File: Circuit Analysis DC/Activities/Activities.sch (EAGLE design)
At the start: 9 parts, among them U1 SWITCH-SPST-2TV

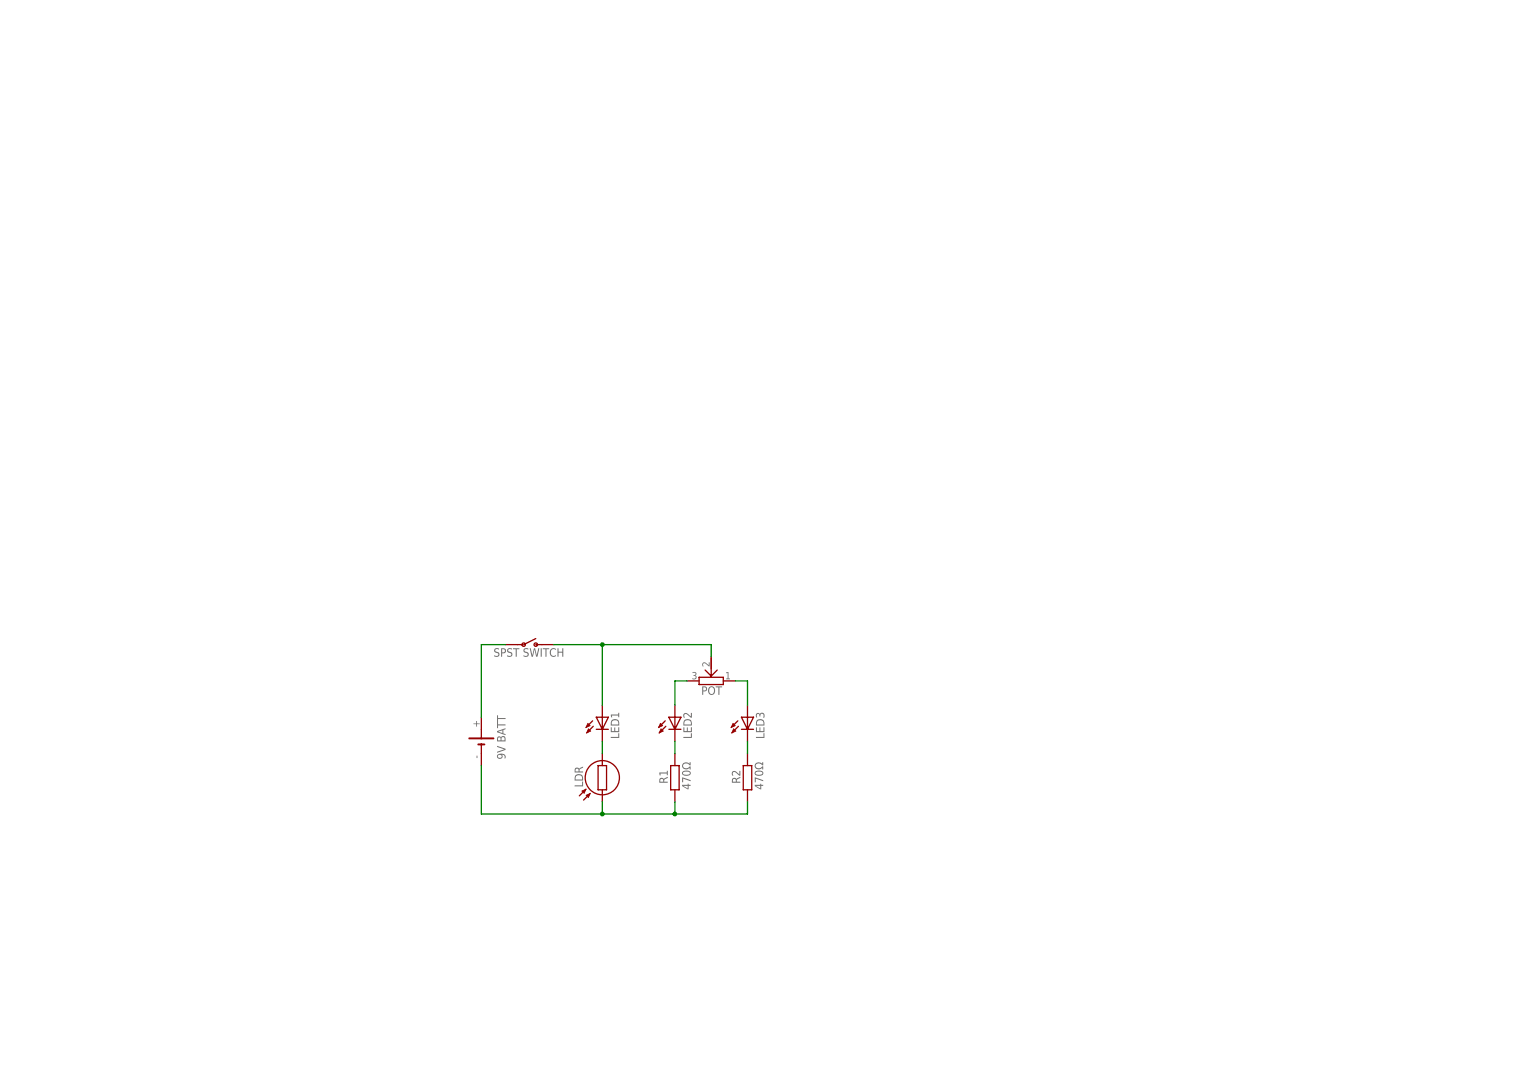
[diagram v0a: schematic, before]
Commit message: added descriptions and thumbnails for website
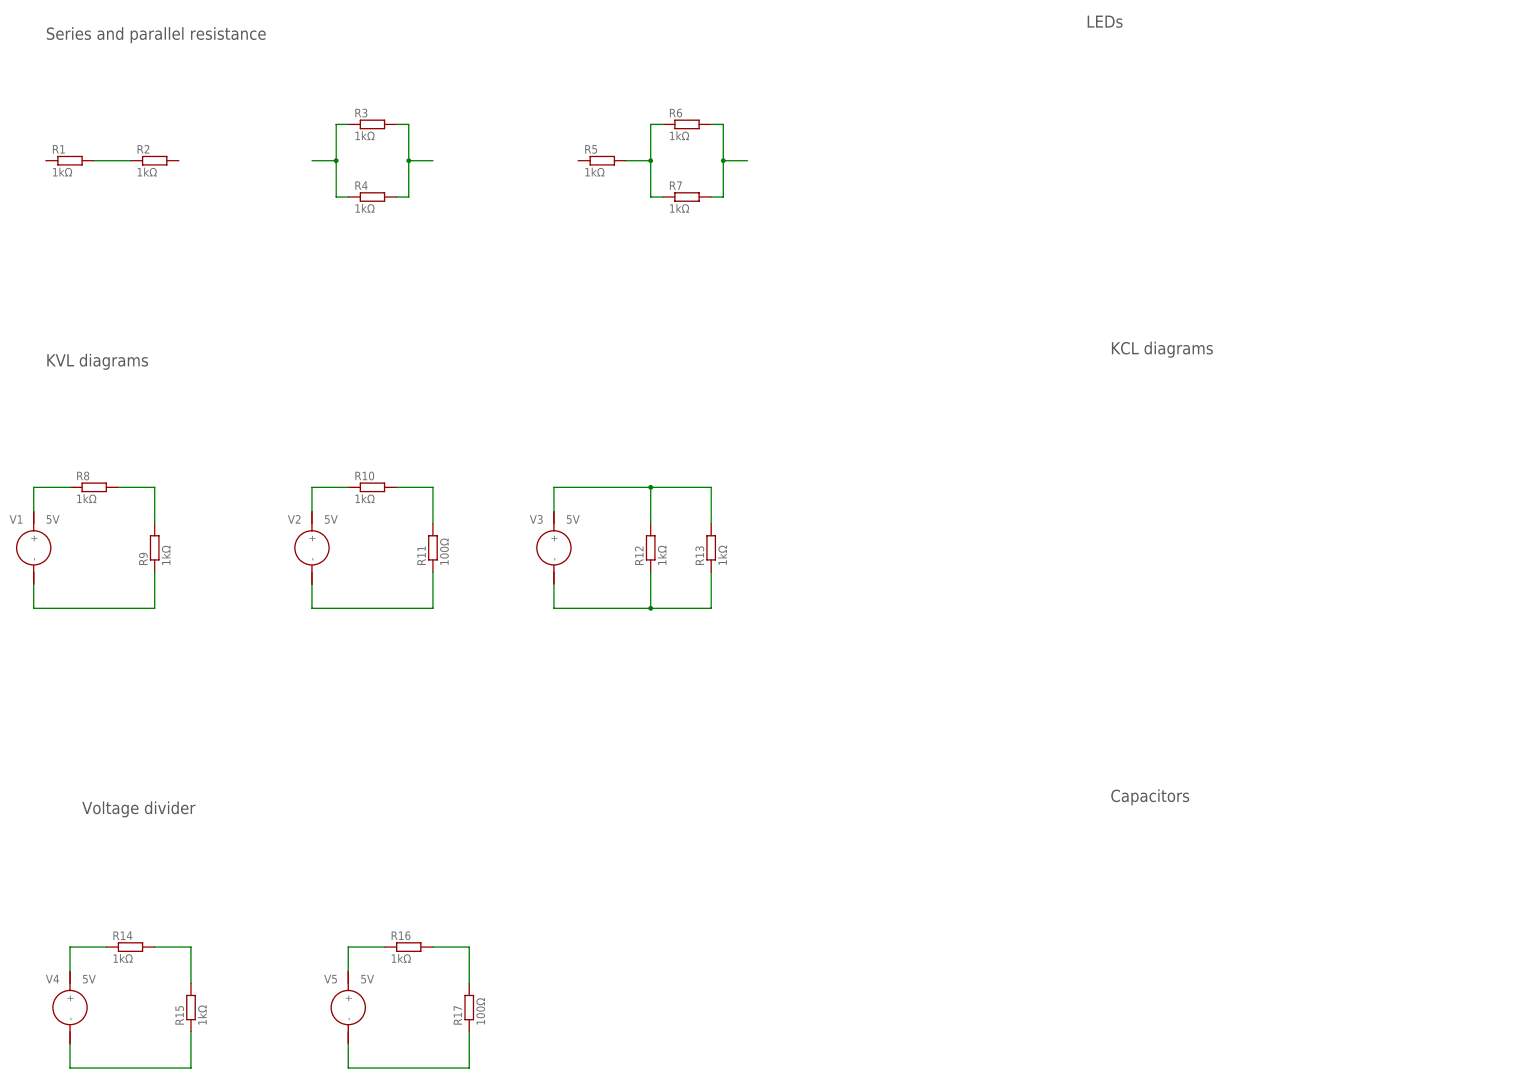
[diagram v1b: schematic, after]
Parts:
- removed G1: BATT_9V, personal:BATT_9V
- removed LDR: LDR_THRU, personal:LDR_THRU
- removed LED1, LED2, LED3: (no value), adafruit:LED5MM
- removed POT: POTENTIOMETER_THRU, personal:POTENTIOMETER_THRU
- removed U1: SWITCH-SPST-2TV, personal:SWITCH-SPST-2TV
- added R10, R12, R13, R14, R15, R16, R3, R4, R5, R6, R7, R8, R9: 1kΩ, rcl:R-EU_0207/10
- added R11, R17: 100Ω, rcl:R-EU_0207/10
- added V1, V2, V3, V4, V5: 5V, personal:VOLTAGE_SOURCE
- R1, R2: value 470Ω -> 1kΩ; device resistor:R-EU_0207/10 -> rcl:R-EU_0207/10
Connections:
- new net N$11: R10.1, V2.+
- new net N$12: R12.2, R13.2, V3.+
- new net N$13: R12.1, R13.1, V3.-
- new net N$14: R14.1, V4.+
- new net N$15: R14.2, R15.2
- new net N$16: R15.1, V4.-
- new net N$17: R17.1, V5.-
- new net N$18: R16.2, R17.2
- new net N$19: R16.1, V5.+
- new net N$4: R5.2, R6.1, R7.1
- new net N$8: R9.1, V1.-
- net N$1: now also R1.2; no longer G1.-, LDR.1, R1.1
- net N$10: now also R10.2, R11.2; no longer LED2.C, R1.2
- net N$2: now also R3.1, R4.1; no longer LED1.A, POT.2, U1.O
- net N$3: now also R3.2, R4.2; no longer LDR.2, LED1.C
- net N$5: now also R6.2, R7.2; no longer LED3.C, R2.2
- net N$6: now also R8.1, V1.+; no longer LED3.A, POT.1
- net N$7: now also R8.2, R9.2; no longer LED2.A, POT.3
- net N$9: now also R11.1, V2.-; no longer G1.+, U1.P
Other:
- note added: "Capacitors"
- note added: "KCL diagrams"
- note added: "KVL diagrams"
- note added: "LEDs"
- note added: "Series and parallel resistance"
- note added: "Voltage divider"
- note removed: "9V BATT"
- note removed: "SPST SWITCH"
- moved on the sheet: R1, R2

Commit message: changed schematic and code
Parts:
- added C1: (no value), rcl:C-EU025-025X050
- added LED1, LED2: (no value), led:LED3MM
- added R18, R19, R20, R22: 1kΩ, rcl:R-EU_0207/10
- added R21: 10kΩ, rcl:R-EU_0207/10
- added U$1: SPDT, another:SPDT
- added V6, V7, V8: 5V, personal:VOLTAGE_SOURCE
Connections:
- new net N$20: R22.2, U$1.B, V8.-
- new net N$21: U$1.IN, V8.+
- new net N$22: C1.1, U$1.A
- new net N$23: C1.2, LED1.A, LED2.C
- new net N$25: LED1.C, LED2.A, R22.1
- new net N$26: R18.2, R19.2, V6.+
- new net N$27: R18.1, R19.1, V6.-
- new net N$28: R20.2, R21.2, V7.+
- new net N$29: R20.1, R21.1, V7.-
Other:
- note added: "SPST SWITCH"
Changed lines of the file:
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@@
 <part name="V4" library="personal" deviceset="VOLTAGE_SOURCE" device="" value="5V"/>
 <part name="V5" library="personal" deviceset="VOLTAGE_SOURCE" device="" value="5V"/>
+<part name="R18" library="rcl" deviceset="R-EU_" device="0207/10" value="1kΩ"/>
+<part name="R19" library="rcl" deviceset="R-EU_" device="0207/10" value="1kΩ"/>
+<part name="R20" library="rcl" deviceset="R-EU_" device="0207/10" value="1kΩ"/>
+<part name="R21" library="rcl" deviceset="R-EU_" device="0207/10" value="10kΩ"/>
+<part name="R22" library="rcl" deviceset="R-EU_" device="0207/10" value="1kΩ"/>
+<part name="V6" library="personal" deviceset="VOLTAGE_SOURCE" device="" value="5V"/>
+<part name="V7" library="personal" deviceset="VOLTAGE_SOURCE" device="" value="5V"/>
+<part name="V8" library="personal" deviceset="VOLTAGE_SOURCE" device="" value="5V"/>
+<part name="C1" library="rcl" deviceset="C-EU" device="025-025X050"/>
+<part name="LED1" library="led" deviceset="LED" device="3MM"/>
+<part name="LED2" library="led" deviceset="LED" device="3MM"/>
+<part name="U$1" library="another" deviceset="SPDT" device=""/>
 </parts>
 <sheets>
@@
 <text x="243.84" y="193.04" size="2.54" layer="97">KCL diagrams</text>
 <text x="238.76" y="261.62" size="2.54" layer="97">LEDs</text>
-<text x="243.84" y="99.06" size="2.54" layer="97">Capacitors</text>
+<text x="243.84" y="101.6" size="2.54" layer="97">Capacitors</text>
 <text x="27.94" y="96.52" size="2.54" layer="97">Voltage divider</text>
+<text x="292.1" y="96.52" size="1.778" layer="95">SPST SWITCH</text>
 </plain>
 <instances>
@@
 <instance part="V4" gate="V$1" x="25.4" y="55.88"/>
 <instance part="V5" gate="V$1" x="83.82" y="55.88"/>
+<instance part="R18" gate="G$1" x="261.62" y="157.48" rot="R90"/>
+<instance part="R19" gate="G$1" x="274.32" y="157.48" rot="R90"/>
+<instance part="R20" gate="G$1" x="314.96" y="157.48" rot="R90"/>
+<instance part="R21" gate="G$1" x="327.66" y="157.48" rot="R90"/>
+<instance part="R22" gate="G$1" x="281.94" y="58.42" rot="R180"/>
+<instance part="V6" gate="V$1" x="241.3" y="157.48"/>
+<instance part="V7" gate="V$1" x="294.64" y="157.48"/>
+<instance part="V8" gate="V$1" x="236.22" y="73.66"/>
+<instance part="C1" gate="G$1" x="299.72" y="83.82"/>
+<instance part="LED1" gate="G$1" x="292.1" y="68.58"/>
+<instance part="LED2" gate="G$1" x="307.34" y="66.04" rot="R180"/>
+<instance part="U$1" gate="G$1" x="256.54" y="88.9" smashed="yes"/>
 </instances>
 <busses>
@@
 </segment>
 </net>
+<net name="N$20" class="0">
+<segment>
+<pinref part="V8" gate="V$1" pin="-"/>
+<wire x1="236.22" y1="66.04" x2="236.22" y2="58.42" width="0.1524" layer="91"/>
+<pinref part="R22" gate="G$1" pin="2"/>
+<wire x1="236.22" y1="58.42" x2="271.78" y2="58.42" width="0.1524" layer="91"/>
+<pinref part="U$1" gate="G$1" pin="B"/>
+<wire x1="271.78" y1="58.42" x2="276.86" y2="58.42" width="0.1524" layer="91"/>
+<wire x1="266.7" y1="83.82" x2="271.78" y2="83.82" width="0.1524" layer="91"/>
+<wire x1="271.78" y1="83.82" x2="271.78" y2="58.42" width="0.1524" layer="91"/>
+<junction x="271.78" y="58.42"/>
+</segment>
+</net>
+<net name="N$21" class="0">
+<segment>
+<pinref part="V8" gate="V$1" pin="+"/>
+<wire x1="236.22" y1="81.28" x2="236.22" y2="88.9" width="0.1524" layer="91"/>
+<pinref part="U$1" gate="G$1" pin="IN"/>
+<wire x1="236.22" y1="88.9" x2="246.38" y2="88.9" width="0.1524" layer="91"/>
+</segment>
+</net>
+<net name="N$22" class="0">
+<segment>
+<pinref part="C1" gate="G$1" pin="1"/>
+<pinref part="U$1" gate="G$1" pin="A"/>
+<wire x1="266.7" y1="93.98" x2="299.72" y2="93.98" width="0.1524" layer="91"/>
+<wire x1="299.72" y1="93.98" x2="299.72" y2="86.36" width="0.1524" layer="91"/>
+</segment>
+</net>
+<net name="N$23" class="0">
+<segment>
+<pinref part="LED1" gate="G$1" pin="A"/>
+<wire x1="292.1" y1="71.12" x2="292.1" y2="76.2" width="0.1524" layer="91"/>
+<pinref part="C1" gate="G$1" pin="2"/>
+<wire x1="292.1" y1="76.2" x2="299.72" y2="76.2" width="0.1524" layer="91"/>
+<wire x1="299.72" y1="76.2" x2="299.72" y2="78.74" width="0.1524" layer="91"/>
+<pinref part="LED2" gate="G$1" pin="C"/>
+<wire x1="307.34" y1="71.12" x2="307.34" y2="76.2" width="0.1524" layer="91"/>
+<wire x1="307.34" y1="76.2" x2="299.72" y2="76.2" width="0.1524" layer="91"/>
+<junction x="299.72" y="76.2"/>
+</segment>
+</net>
+<net name="N$25" class="0">
+<segment>
+<pinref part="LED2" gate="G$1" pin="A"/>
+<wire x1="307.34" y1="63.5" x2="307.34" y2="58.42" width="0.1524" layer="91"/>
+<pinref part="R22" gate="G$1" pin="1"/>
+<wire x1="307.34" y1="58.42" x2="292.1" y2="58.42" width="0.1524" layer="91"/>
+<pinref part="LED1" gate="G$1" pin="C"/>
+<wire x1="292.1" y1="58.42" x2="287.02" y2="58.42" width="0.1524" layer="91"/>
+<wire x1="292.1" y1="63.5" x2="292.1" y2="58.42" width="0.1524" layer="91"/>
+<junction x="292.1" y="58.42"/>
+</segment>
+</net>
+<net name="N$26" class="0">
+<segment>
+<pinref part="V6" gate="V$1" pin="+"/>
+<wire x1="241.3" y1="165.1" x2="241.3" y2="167.64" width="0.1524" layer="91"/>
+<pinref part="R19" gate="G$1" pin="2"/>
+<wire x1="241.3" y1="167.64" x2="261.62" y2="167.64" width="0.1524" layer="91"/>
+<wire x1="261.62" y1="167.64" x2="274.32" y2="167.64" width="0.1524" layer="91"/>
+<wire x1="274.32" y1="167.64" x2="274.32" y2="162.56" width="0.1524" layer="91"/>
+<pinref part="R18" gate="G$1" pin="2"/>
+<wire x1="261.62" y1="162.56" x2="261.62" y2="167.64" width="0.1524" layer="91"/>
+<junction x="261.62" y="167.64"/>
+</segment>
+</net>
+<net name="N$27" class="0">
+<segment>
+<pinref part="R19" gate="G$1" pin="1"/>
+<wire x1="274.32" y1="152.4" x2="274.32" y2="147.32" width="0.1524" layer="91"/>
+<pinref part="V6" gate="V$1" pin="-"/>
+<wire x1="274.32" y1="147.32" x2="261.62" y2="147.32" width="0.1524" layer="91"/>
+<wire x1="261.62" y1="147.32" x2="241.3" y2="147.32" width="0.1524" layer="91"/>
+<wire x1="241.3" y1="147.32" x2="241.3" y2="149.86" width="0.1524" layer="91"/>
+<pinref part="R18" gate="G$1" pin="1"/>
+<wire x1="261.62" y1="152.4" x2="261.62" y2="147.32" width="0.1524" layer="91"/>
+<junction x="261.62" y="147.32"/>
+</segment>
+</net>
+<net name="N$28" class="0">
+<segment>
+<pinref part="V7" gate="V$1" pin="+"/>
+<wire x1="294.64" y1="165.1" x2="294.64" y2="167.64" width="0.1524" layer="91"/>
+<pinref part="R21" gate="G$1" pin="2"/>
+<wire x1="294.64" y1="167.64" x2="314.96" y2="167.64" width="0.1524" layer="91"/>
+<wire x1="314.96" y1="167.64" x2="327.66" y2="167.64" width="0.1524" layer="91"/>
+<wire x1="327.66" y1="167.64" x2="327.66" y2="162.56" width="0.1524" layer="91"/>
+<pinref part="R20" gate="G$1" pin="2"/>
+<wire x1="314.96" y1="162.56" x2="314.96" y2="167.64" width="0.1524" layer="91"/>
+<junction x="314.96" y="167.64"/>
+</segment>
+</net>
+<net name="N$29" class="0">
+<segment>
+<pinref part="R21" gate="G$1" pin="1"/>
+<wire x1="327.66" y1="152.4" x2="327.66" y2="147.32" width="0.1524" layer="91"/>
+<pinref part="V7" gate="V$1" pin="-"/>
+<wire x1="327.66" y1="147.32" x2="314.96" y2="147.32" width="0.1524" layer="91"/>
+<wire x1="314.96" y1="147.32" x2="294.64" y2="147.32" width="0.1524" layer="91"/>
+<wire x1="294.64" y1="147.32" x2="294.64" y2="149.86" width="0.1524" layer="91"/>
+<pinref part="R20" gate="G$1" pin="1"/>
+<wire x1="314.96" y1="152.4" x2="314.96" y2="147.32" width="0.1524" layer="91"/>
+<junction x="314.96" y="147.32"/>
+</segment>
+</net>
